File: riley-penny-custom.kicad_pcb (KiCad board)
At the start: 2 copper layers, 110 x 84.3 mm, 4 parts, among them J1 Barrel_Jack_Switch, J2 AudioJack_TRS, J3 AudioJack_TRS

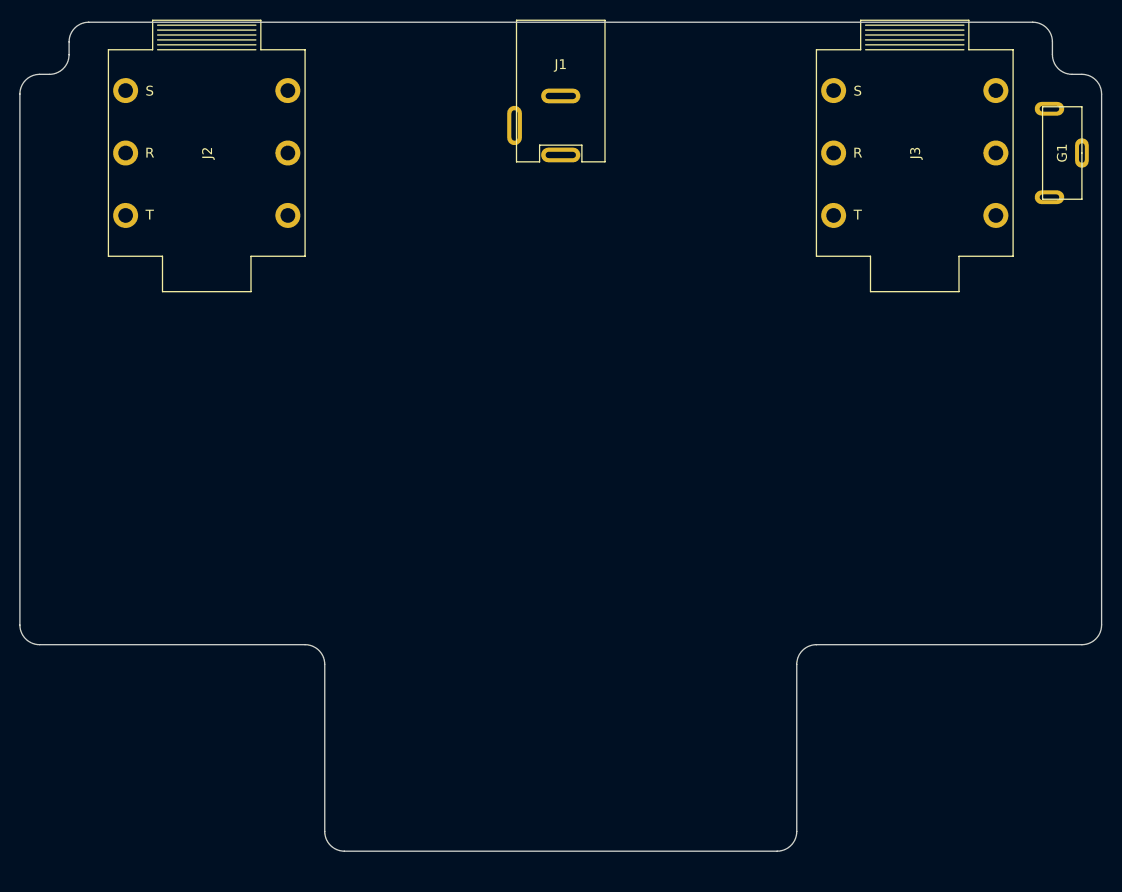
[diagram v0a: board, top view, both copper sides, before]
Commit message: finished schematics, started PCB
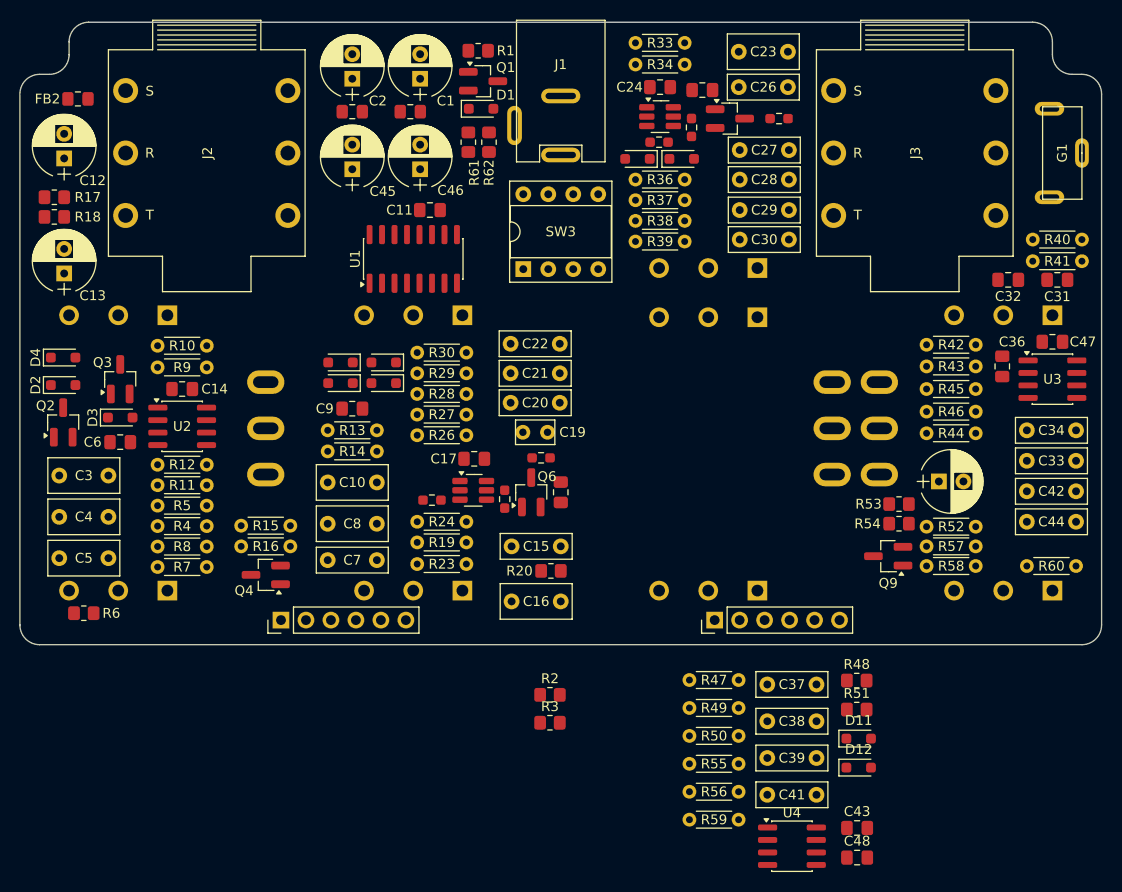
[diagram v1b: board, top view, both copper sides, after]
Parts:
- added C1: 100uF, bca-footprints:CP_Radial_D6.3mm_P2.50mm, F.Cu at (-14.3, -38.8)
- added C10: 0.47uF, bca-footprints:C_Film_L7.2mm_W3.5mm_P5.00mm, F.Cu at (-21.2, 3.50)
- added C11: 1u, Capacitor_SMD:C_0805_2012Metric_Pad1.18x1.45mm_HandSolder, F.Cu at (-13.3, -24.2)
- added C12: 100u, bca-footprints:CP_Radial_D6.3mm_P2.50mm, F.Cu at (-50.5, -30.7)
- added C13: 100u, bca-footprints:CP_Radial_D6.3mm_P2.50mm, F.Cu at (-50.5, -19.0)
- added C14: 100n, Capacitor_SMD:C_0805_2012Metric_Pad1.18x1.45mm_HandSolder, F.Cu at (-38.5, -6.00)
- added C15: 10n, bca-footprints:C_Film_L7.2mm_W2.5mm_P5.00mm, F.Cu at (-2.50, 10.0)
- added C16: 0.15u, bca-footprints:C_Film_L7.2mm_W3.5mm_P5.00mm, F.Cu at (-2.50, 15.6)
- added C17: 47p, Capacitor_SMD:C_0805_2012Metric_Pad1.18x1.45mm_HandSolder, F.Cu at (-8.80, 1.10)
- added C18: 47p, Capacitor_SMD:C_0805_2012Metric_Pad1.18x1.45mm_HandSolder, F.Cu at (0.00, 4.50)
- added C19: 220p, bca-footprints:C_Ceramic_L4.0mm_W2.5mm_P2.50mm, F.Cu at (-2.60, -1.60)
- added C2: 100uF, bca-footprints:CP_Radial_D6.3mm_P2.50mm, F.Cu at (-21.2, -38.8)
- added C20: 0.1u, bca-footprints:C_Film_L7.2mm_W2.5mm_P5.00mm, F.Cu at (-2.60, -4.60)
- added C21: 47n, bca-footprints:C_Film_L7.2mm_W2.5mm_P5.00mm, F.Cu at (-2.60, -7.60)
- added C22: 3.9n, bca-footprints:C_Film_L7.2mm_W2.5mm_P5.00mm, F.Cu at (-2.60, -10.6)
- added C23: 0.47u, bca-footprints:C_Film_L7.2mm_W3.5mm_P5.00mm, F.Cu at (20.6, -40.3)
- added C24: 100p, Capacitor_SMD:C_0805_2012Metric_Pad1.18x1.45mm_HandSolder, F.Cu at (10.1, -36.7)
- added C25: 100p, Capacitor_SMD:C_0805_2012Metric_Pad1.18x1.45mm_HandSolder, F.Cu at (14.4, -36.4)
- added C26: 5.6n, bca-footprints:C_Film_L7.2mm_W2.5mm_P5.00mm, F.Cu at (20.6, -36.7)
- added C27: 5.6n, bca-footprints:C_Film_L7.2mm_W2.5mm_P5.00mm, F.Cu at (20.7, -30.3)
- added C28: 18n, bca-footprints:C_Film_L7.2mm_W2.5mm_P5.00mm, F.Cu at (20.7, -27.3)
- added C29: 68n, bca-footprints:C_Film_L7.2mm_W2.5mm_P5.00mm, F.Cu at (20.7, -24.2)
- added C3: 0.47u, bca-footprints:C_Film_L7.2mm_W3.5mm_P5.00mm, F.Cu at (-48.5, 2.80)
- added C30: 33n, bca-footprints:C_Film_L7.2mm_W2.5mm_P5.00mm, F.Cu at (20.7, -21.2)
- added C31: 22p, Capacitor_SMD:C_0805_2012Metric_Pad1.18x1.45mm_HandSolder, F.Cu at (50.5, -17.1)
- added C32: 10u, Capacitor_SMD:C_0805_2012Metric_Pad1.18x1.45mm_HandSolder, F.Cu at (45.5, -17.1)
- added C33: 8.2n, bca-footprints:C_Film_L7.2mm_W2.5mm_P5.00mm, F.Cu at (49.9, 1.30)
- added C34: 5.6n, bca-footprints:C_Film_L7.2mm_W2.5mm_P5.00mm, F.Cu at (49.9, -1.80)
- added C36: 47p, Capacitor_SMD:C_0805_2012Metric_Pad1.18x1.45mm_HandSolder, F.Cu at (44.9, -8.30)
- added C37: 47n, bca-footprints:C_Film_L7.2mm_W2.5mm_P5.00mm, F.Cu at (23.5, 24.0)
- added C38: 8.2n, bca-footprints:C_Film_L7.2mm_W2.5mm_P5.00mm, F.Cu at (23.5, 27.8)
- added C39: 18n, bca-footprints:C_Film_L7.2mm_W2.5mm_P5.00mm, F.Cu at (23.5, 31.5)
- added C4: 0.22u, bca-footprints:C_Film_L7.2mm_W3.5mm_P5.00mm, F.Cu at (-48.5, 7.00)
- added C40: 100u, bca-footprints:CP_Radial_D6.3mm_P2.50mm, F.Cu at (39.7, 3.40)
- added C41: 3.9n, bca-footprints:C_Film_L7.2mm_W2.5mm_P5.00mm, F.Cu at (23.5, 35.3)
- added C42: 39n, bca-footprints:C_Film_L7.2mm_W2.5mm_P5.00mm, F.Cu at (49.9, 4.40)
- added C43: 10u, Capacitor_SMD:C_0805_2012Metric_Pad1.18x1.45mm_HandSolder, F.Cu at (30.1, 38.6)
- added C44: 5.6n, bca-footprints:C_Film_L7.2mm_W2.5mm_P5.00mm, F.Cu at (49.9, 7.50)
- added C45: 100u, bca-footprints:CP_Radial_D6.3mm_P2.50mm, F.Cu at (-21.2, -29.6)
- added C46: 100u, bca-footprints:CP_Radial_D6.3mm_P2.50mm, F.Cu at (-14.3, -29.6)
- added C47: 100n, Capacitor_SMD:C_0805_2012Metric_Pad1.18x1.45mm_HandSolder, F.Cu at (50.0, -10.8)
- added C48: 100n, Capacitor_SMD:C_0805_2012Metric_Pad1.18x1.45mm_HandSolder, F.Cu at (30.1, 41.6)
- added C5: 0.22u, bca-footprints:C_Film_L7.2mm_W3.5mm_P5.00mm, F.Cu at (-48.5, 11.2)
- added C6: 100p, Capacitor_SMD:C_0805_2012Metric_Pad1.18x1.45mm_HandSolder, F.Cu at (-44.8, -0.60)
- added C7: 3.3nF, bca-footprints:C_Film_L7.2mm_W2.5mm_P5.00mm, F.Cu at (-21.2, 11.4)
- added C8: 0.22uF, bca-footprints:C_Film_L7.2mm_W3.5mm_P5.00mm, F.Cu at (-21.2, 7.70)
- added C9: 470p, Capacitor_SMD:C_0805_2012Metric_Pad1.18x1.45mm_HandSolder, F.Cu at (-21.2, -4.00)
- added D1: 9V1 Zener, Diode_SMD:D_SOD-323_HandSoldering, F.Cu at (-8.10, -34.5)
- added D10: 3v3 Zener, Diode_SMD:D_SOD-323_HandSoldering, F.Cu at (7.80, -29.4)
- added D11: 1N4148, Diode_SMD:D_SOD-323_HandSoldering, F.Cu at (30.3, 29.6)
- added D12: 1N4148, Diode_SMD:D_SOD-323_HandSoldering, F.Cu at (30.3, 32.5)
- added D2: 1N5711, Diode_SMD:D_SOD-323_HandSoldering, F.Cu at (-50.6, -6.40)
- added D3: 1N5711, Diode_SMD:D_SOD-323_HandSoldering, F.Cu at (-44.8, -3.10)
- added D4: 1N5711, Diode_SMD:D_SOD-323_HandSoldering, F.Cu at (-50.6, -9.20)
- added D5: 1N4148, Diode_SMD:D_SOD-323_HandSoldering, F.Cu at (-18.0, -6.60)
- added D6: 1N5711, Diode_SMD:D_SOD-323_HandSoldering, F.Cu at (-22.4, -6.60)
- added D7: 1N4148, Diode_SMD:D_SOD-323_HandSoldering, F.Cu at (-18.0, -8.70)
- added D8: 1N4148, Diode_SMD:D_SOD-323_HandSoldering, F.Cu at (-22.4, -8.70)
- added D9: 3v3 Zener, Diode_SMD:D_SOD-323_HandSoldering, F.Cu at (12.3, -29.4)
- added FB1: FerriteBead_Small, Inductor_SMD:L_0805_2012Metric_Pad1.15x1.40mm_HandSolder, F.Cu at (-15.3, -34.2)
- added FB2: FerriteBead_Small, Inductor_SMD:L_0805_2012Metric_Pad1.15x1.40mm_HandSolder, F.Cu at (-49.1, -35.5)
- added FB3: FerriteBead_Small, Inductor_SMD:L_0805_2012Metric_Pad1.15x1.40mm_HandSolder, F.Cu at (-21.2, -34.2)
- added J4: Conn_01x06, bca-footprints:Pin_Header_Straight_1x06_Pitch2.54mm, F.Cu at (-22.1, 17.5)
- added J5: Conn_01x06, bca-footprints:Pin_Header_Straight_1x06_Pitch2.54mm, F.Cu at (22.0, 17.5)
- added Q1: Q_PMOS_GSD, Package_TO_SOT_SMD:SOT-23_Handsoldering, F.Cu at (-7.90, -37.3)
- added Q2: 2N7002, Package_TO_SOT_SMD:SOT-23_Handsoldering, F.Cu at (-50.6, -2.60)
- added Q3: 2N7002, Package_TO_SOT_SMD:SOT-23_Handsoldering, F.Cu at (-44.8, -7.00)
- added Q4: 2N7002, Package_TO_SOT_SMD:SOT-23_Handsoldering, F.Cu at (-30.0, 12.9)
- added Q5: LS844, Package_TO_SOT_SMD:SOT-23-6_Handsoldering, F.Cu at (-8.90, 4.30)
- added Q6: BC858C, Package_TO_SOT_SMD:SOT-23_Handsoldering, F.Cu at (-3.00, 4.50)
- added Q7: LS844, Package_TO_SOT_SMD:SOT-23-6_Handsoldering, F.Cu at (10.1, -33.7)
- added Q8: BC858C, Package_TO_SOT_SMD:SOT-23_Handsoldering, F.Cu at (17.2, -33.5)
- added Q9: BC848C, Package_TO_SOT_SMD:SOT-23_Handsoldering, F.Cu at (33.3, 11.0)
- added R1: 10k, Resistor_SMD:R_0805_2012Metric_Pad1.20x1.40mm_HandSolder, F.Cu at (-8.40, -40.4)
- added R10: 10k, bca-footprints:R_L3.6mm_D1.6mm_P5.00mm_Horizontal, F.Cu at (-38.5, -10.4)
- added R11: 10k, bca-footprints:R_L3.6mm_D1.6mm_P5.00mm_Horizontal, F.Cu at (-38.5, 3.78)
- added R12: 18k, bca-footprints:R_L3.6mm_D1.6mm_P5.00mm_Horizontal, F.Cu at (-38.5, 1.70)
- added R13: 10k, bca-footprints:R_L3.6mm_D1.6mm_P5.00mm_Horizontal, F.Cu at (-21.2, -1.80)
- added R14: 1k, bca-footprints:R_L3.6mm_D1.6mm_P5.00mm_Horizontal, F.Cu at (-21.2, 0.34)
- added R15: 100k, bca-footprints:R_L3.6mm_D1.6mm_P5.00mm_Horizontal, F.Cu at (-30.0, 7.90)
- added R16: 100k, bca-footprints:R_L3.6mm_D1.6mm_P5.00mm_Horizontal, F.Cu at (-30.0, 10.0)
- added R17: 10k, Resistor_SMD:R_0805_2012Metric_Pad1.20x1.40mm_HandSolder, F.Cu at (-51.5, -25.5)
- added R18: 10k, Resistor_SMD:R_0805_2012Metric_Pad1.20x1.40mm_HandSolder, F.Cu at (-51.5, -23.5)
- added R19: 10k, bca-footprints:R_L3.6mm_D1.6mm_P5.00mm_Horizontal, F.Cu at (-12.1, 9.60)
- added R2: 22k, Resistor_SMD:R_0805_2012Metric_Pad1.20x1.40mm_HandSolder, F.Cu at (-1.10, 25.1)
- added R20: 1M, Resistor_SMD:R_0805_2012Metric_Pad1.20x1.40mm_HandSolder, F.Cu at (-1.00, 12.5)
- added R21: 2.2k, Resistor_SMD:R_0603_1608Metric_Pad0.98x0.95mm_HandSolder, F.Cu at (-5.70, 5.20)
- added R22: 4.7k, Resistor_SMD:R_0603_1608Metric_Pad0.98x0.95mm_HandSolder, F.Cu at (-13.1, 5.30)
- added R23: 1.5k, bca-footprints:R_L3.6mm_D1.6mm_P5.00mm_Horizontal, F.Cu at (-12.1, 11.8)
- added R24: 15k, bca-footprints:R_L3.6mm_D1.6mm_P5.00mm_Horizontal, F.Cu at (-12.1, 7.50)
- added R25: 2.2k, Resistor_SMD:R_0603_1608Metric_Pad0.98x0.95mm_HandSolder, F.Cu at (-2.00, 1.00)
- added R26: 56k, bca-footprints:R_L3.6mm_D1.6mm_P5.00mm_Horizontal, F.Cu at (-12.1, -1.30)
- added R27: 330k, bca-footprints:R_L3.6mm_D1.6mm_P5.00mm_Horizontal, F.Cu at (-12.1, -3.40)
- added R28: 1M, bca-footprints:R_L3.6mm_D1.6mm_P5.00mm_Horizontal, F.Cu at (-12.1, -5.50)
- added R29: 15k, bca-footprints:R_L3.6mm_D1.6mm_P5.00mm_Horizontal, F.Cu at (-12.1, -7.60)
- added R3: 22k, Resistor_SMD:R_0805_2012Metric_Pad1.20x1.40mm_HandSolder, F.Cu at (-1.10, 27.9)
- added R30: 470k, bca-footprints:R_L3.6mm_D1.6mm_P5.00mm_Horizontal, F.Cu at (-12.1, -9.70)
- added R31: 2.2k, Resistor_SMD:R_0603_1608Metric_Pad0.98x0.95mm_HandSolder, F.Cu at (13.3, -32.6)
- added R32: 4.7k, Resistor_SMD:R_0603_1608Metric_Pad0.98x0.95mm_HandSolder, F.Cu at (10.0, -31.1)
- added R33: 3.9k, bca-footprints:R_L3.6mm_D1.6mm_P5.00mm_Horizontal, F.Cu at (10.1, -41.2)
- added R34: 33k, bca-footprints:R_L3.6mm_D1.6mm_P5.00mm_Horizontal, F.Cu at (10.1, -39.0)
- added R35: 2.2k, Resistor_SMD:R_0603_1608Metric_Pad0.98x0.95mm_HandSolder, F.Cu at (22.2, -33.5)
- added R36: 1k, bca-footprints:R_L3.6mm_D1.6mm_P5.00mm_Horizontal, F.Cu at (10.1, -27.3)
- added R37: 6.8k, bca-footprints:R_L3.6mm_D1.6mm_P5.00mm_Horizontal, F.Cu at (10.1, -25.2)
- added R38: 5.6k, bca-footprints:R_L3.6mm_D1.6mm_P5.00mm_Horizontal, F.Cu at (10.1, -23.1)
- added R39: 3.9k, bca-footprints:R_L3.6mm_D1.6mm_P5.00mm_Horizontal, F.Cu at (10.1, -21.0)
- added R4: 2.2M, bca-footprints:R_L3.6mm_D1.6mm_P5.00mm_Horizontal, F.Cu at (-38.5, 7.94)
- added R40: 470k, bca-footprints:R_L3.6mm_D1.6mm_P5.00mm_Horizontal, F.Cu at (50.5, -21.2)
- added R41: 180k, bca-footprints:R_L3.6mm_D1.6mm_P5.00mm_Horizontal, F.Cu at (50.5, -19.0)
- added R42: 10k, bca-footprints:R_L3.6mm_D1.6mm_P5.00mm_Horizontal, F.Cu at (39.7, -10.5)
- added R43: 22k, bca-footprints:R_L3.6mm_D1.6mm_P5.00mm_Horizontal, F.Cu at (39.7, -8.30)
- added R44: 15k, bca-footprints:R_L3.6mm_D1.6mm_P5.00mm_Horizontal, F.Cu at (39.7, -1.50)
- added R45: 10k, bca-footprints:R_L3.6mm_D1.6mm_P5.00mm_Horizontal, F.Cu at (39.7, -6.00)
- added R46: 22k, bca-footprints:R_L3.6mm_D1.6mm_P5.00mm_Horizontal, F.Cu at (39.7, -3.70)
- added R47: 1.5k, bca-footprints:R_L3.6mm_D1.6mm_P5.00mm_Horizontal, F.Cu at (15.6, 23.6)
- added R48: 1M, Resistor_SMD:R_0805_2012Metric_Pad1.20x1.40mm_HandSolder, F.Cu at (30.1, 23.6)
- added R49: 470k, bca-footprints:R_L3.6mm_D1.6mm_P5.00mm_Horizontal, F.Cu at (15.6, 26.4)
- added R5: 470k, bca-footprints:R_L3.6mm_D1.6mm_P5.00mm_Horizontal, F.Cu at (-38.5, 5.86)
- added R50: 1k, bca-footprints:R_L3.6mm_D1.6mm_P5.00mm_Horizontal, F.Cu at (15.6, 29.3)
- added R51: 1M, Resistor_SMD:R_0805_2012Metric_Pad1.20x1.40mm_HandSolder, F.Cu at (30.1, 26.6)
- added R52: 22k, bca-footprints:R_L3.6mm_D1.6mm_P5.00mm_Horizontal, F.Cu at (39.7, 8.00)
- added R53: 1M, Resistor_SMD:R_0805_2012Metric_Pad1.20x1.40mm_HandSolder, F.Cu at (34.4, 5.70)
- added R54: 1M, Resistor_SMD:R_0805_2012Metric_Pad1.20x1.40mm_HandSolder, F.Cu at (34.4, 7.70)
- added R55: 6.8k, bca-footprints:R_L3.6mm_D1.6mm_P5.00mm_Horizontal, F.Cu at (15.6, 32.1)
- added R56: 100k, bca-footprints:R_L3.6mm_D1.6mm_P5.00mm_Horizontal, F.Cu at (15.6, 35.0)
- added R57: 470k, bca-footprints:R_L3.6mm_D1.6mm_P5.00mm_Horizontal, F.Cu at (39.7, 10.0)
- added R58: 1k, bca-footprints:R_L3.6mm_D1.6mm_P5.00mm_Horizontal, F.Cu at (39.7, 12.0)
- added R59: 10k, bca-footprints:R_L3.6mm_D1.6mm_P5.00mm_Horizontal, F.Cu at (15.6, 37.8)
- added R6: 10M, Resistor_SMD:R_0805_2012Metric_Pad1.20x1.40mm_HandSolder, F.Cu at (-48.5, 16.8)
- added R60: 10k, bca-footprints:R_L3.6mm_D1.6mm_P5.00mm_Horizontal, F.Cu at (49.9, 12.0)
- added R61: 10k, Resistor_SMD:R_0805_2012Metric_Pad1.20x1.40mm_HandSolder, F.Cu at (-9.40, -31.1)
- added R62: 10k, Resistor_SMD:R_0805_2012Metric_Pad1.20x1.40mm_HandSolder, F.Cu at (-7.30, -31.1)
- added R7: 10k, bca-footprints:R_L3.6mm_D1.6mm_P5.00mm_Horizontal, F.Cu at (-38.5, 12.1)
- added R8: 1k, bca-footprints:R_L3.6mm_D1.6mm_P5.00mm_Horizontal, F.Cu at (-38.5, 10.0)
- added R9: 680k, bca-footprints:R_L3.6mm_D1.6mm_P5.00mm_Horizontal, F.Cu at (-38.5, -8.20)
- added RV1: 10kC, bca-footprints:R_POT, F.Cu at (-45.0, -2.00)
- added RV2: 1MA, bca-footprints:R_POT, F.Cu at (-45.0, -30.0)
- added RV3: 50kB, bca-footprints:R_POT, F.Cu at (-15.0, -2.00)
- added RV4: 100kA, bca-footprints:R_POT, F.Cu at (-15.0, -30.0)
- added RV5: 250kA, bca-footprints:R_POT_DUAL, F.Cu at (15.0, -30.0)
- added RV6: 100kA, bca-footprints:R_POT, F.Cu at (45.0, -30.0)
- added RV7: 100k-CD, bca-footprints:R_POT, F.Cu at (15.0, -2.00)
- added RV8: 100k-CD, bca-footprints:R_POT, F.Cu at (45.0, -2.00)
- added SW1: SW_SPDT, bca-footprints:SW_Toggle_SPDT_SolderLug, B.Cu at (-30.0, -2.00)
- added SW2: SW_DPDT_x2, bca-footprints:SW_Toggle_DPDT_SolderLug, B.Cu at (30.0, -2.00)
- added SW3: SW_DIP_SPDT_2pos, bca-footprints:DIP-8_W7.62mm_Socket, F.Cu at (0.00, -22.0)
- added U1: DG412xY, Package_SO:SOIC-16_3.9x9.9mm_P1.27mm, F.Cu at (-15.0, -19.2)
- added U2: OPA2134, Package_SO:SOIC-8_3.9x4.9mm_P1.27mm, F.Cu at (-38.5, -2.20)
- added U3: TLV9352, Package_SO:SOIC-8_3.9x4.9mm_P1.27mm, F.Cu at (50.0, -7.00)
- added U4: TLV9352, Package_SO:SOIC-8_3.9x4.9mm_P1.27mm, F.Cu at (23.5, 40.5)
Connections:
- J1 pad 1: Net-(J1-Pad1) -> Earth
- J1 pad 3: Net-(J1-Pad3) -> unconnected-(J1-Pad3)
- J2 pad 2: Net-(J1-Pad1) -> Earth
- J2 pad 5: Net-(J2-Pad5) -> Earth
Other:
- board size 110 x 84.3 mm -> 110 x 63.3 mm

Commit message: initial layout
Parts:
- removed C46: 100u, bca-footprints:CP_Radial_D6.3mm_P2.50mm
- removed C47, C48: 100n, Capacitor_SMD:C_0805_2012Metric_Pad1.18x1.45mm_HandSolder
- removed R62: 10k, Resistor_SMD:R_0805_2012Metric_Pad1.20x1.40mm_HandSolder
- added C35: 47p, Capacitor_SMD:C_0603_1608Metric_Pad1.08x0.95mm_HandSolder, F.Cu at (48.7, -1.20)
- C14, C17, C18, C24, C25, C31, C6, C9: footprint Capacitor_SMD:C_0805_2012Metric_Pad1.18x1.45mm_HandSolder -> Capacitor_SMD:C_0603_1608Metric_Pad1.08x0.95mm_HandSolder
- C23: value 0.47u -> 1u
- C33: value 8.2n -> 5.6n
- C34: value 5.6n -> 8.2n
- C36: value 47p -> 8.2n; footprint Capacitor_SMD:C_0805_2012Metric_Pad1.18x1.45mm_HandSolder -> bca-footprints:C_Film_L7.2mm_W2.5mm_P5.00mm
- C37: value 47n -> 18n
- C38: value 8.2n -> 39n
- C39: value 18n -> 3.9n
- C40: value 100u -> 5.6n; footprint bca-footprints:CP_Radial_D6.3mm_P2.50mm -> bca-footprints:C_Film_L7.2mm_W2.5mm_P5.00mm
- C41: value 3.9n -> 10u; footprint bca-footprints:C_Film_L7.2mm_W2.5mm_P5.00mm -> Capacitor_SMD:C_0805_2012Metric_Pad1.18x1.45mm_HandSolder
- C42: value 39n -> 100u; footprint bca-footprints:C_Film_L7.2mm_W2.5mm_P5.00mm -> bca-footprints:CP_Radial_D6.3mm_P2.50mm
- C43: value 10u -> 100u; footprint Capacitor_SMD:C_0805_2012Metric_Pad1.18x1.45mm_HandSolder -> bca-footprints:CP_Radial_D6.3mm_P2.50mm
- C44: value 5.6n -> 100n; footprint bca-footprints:C_Film_L7.2mm_W2.5mm_P5.00mm -> Capacitor_SMD:C_0603_1608Metric_Pad1.08x0.95mm_HandSolder
- C45: value 100u -> 100n; footprint bca-footprints:CP_Radial_D6.3mm_P2.50mm -> Capacitor_SMD:C_0603_1608Metric_Pad1.08x0.95mm_HandSolder
- D10: value 3v3 Zener -> 4v7 Zener
- R48: value 1M -> 470k; footprint Resistor_SMD:R_0805_2012Metric_Pad1.20x1.40mm_HandSolder -> bca-footprints:R_L3.6mm_D1.6mm_P5.00mm_Horizontal
- R49: value 470k -> 1M; footprint bca-footprints:R_L3.6mm_D1.6mm_P5.00mm_Horizontal -> Resistor_SMD:R_0805_2012Metric_Pad1.20x1.40mm_HandSolder
- R52: value 22k -> 33k; footprint bca-footprints:R_L3.6mm_D1.6mm_P5.00mm_Horizontal -> Resistor_SMD:R_0805_2012Metric_Pad1.20x1.40mm_HandSolder
- R54: value 1M -> 6.8k; footprint Resistor_SMD:R_0805_2012Metric_Pad1.20x1.40mm_HandSolder -> bca-footprints:R_L3.6mm_D1.6mm_P5.00mm_Horizontal
- R55: value 6.8k -> 470k
- R56: value 100k -> 1k
- R57: value 470k -> 100k
- R58: value 1k -> 10k
- R60: footprint bca-footprints:R_L3.6mm_D1.6mm_P5.00mm_Horizontal -> Resistor_SMD:R_0805_2012Metric_Pad1.20x1.40mm_HandSolder
- moved C43 81.4 mm to (-14.3, -29.5), turned to 90 degrees
- moved C42 78.7 mm to (-21.2, -29.4), turned to 90 degrees
- moved R60 73.3 mm to (-9.40, -31.1), turned to 90 degrees
- moved R3 50.8 mm to (-7.30, -22.5), turned to 90 degrees
- moved R2 48.3 mm to (-9.40, -22.5), turned to 90 degrees
- moved U4 46.7 mm to (20.0, -6.10), turned to 90 degrees
- moved C45 43.5 mm to (16.4, -7.70), turned to -90 degrees
- moved R50 42.1 mm to (40.8, -4.40), turned to 180 degrees
- moved R49 41.6 mm to (33.8, -11.0), turned to 90 degrees
- moved R56 38.5 mm to (10.1, -3.20)
- moved C37 38.4 mm to (40.8, -10.2)
- moved R51 37.6 mm to (31.3, -11.0), turned to -90 degrees
- moved R47 36.0 mm to (40.8, -2.17), turned to 180 degrees
- moved C41 35.4 mm to (17.6, 0.40), turned to -90 degrees
- moved R58 34.3 mm to (10.1, -5.40), turned to 180 degrees
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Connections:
- C33 pad 1: Net-(C33-Pad1) -> Net-(U3A--)
- C34 pad 1: Net-(U3A--) -> Net-(C34-Pad1)
- C36 pad 1: Net-(U3A--) -> Net-(U4B-+)
- C37 pad 2: Net-(C37-Pad2) -> Net-(SW2A-C)
- C38 pad 1: Net-(U4B-+) -> Net-(SW2B-A)
- C39 pad 1: Net-(C38-Pad2) -> Net-(D11-K)
- C39 pad 2: Net-(SW2A-C) -> Net-(C39-Pad2)
- C40 pad 1: Net-(SW2B-C) -> Net-(C38-Pad2)
- C40 pad 2: Net-(C40-Pad2) -> Net-(Q9-B)
- C41 pad 1: Net-(D11-K) -> Net-(C39-Pad2)
- C42 pad 1: Net-(SW2B-A) -> /blues-driver/9V
- C42 pad 2: Net-(C42-Pad2) -> Earth
- C43 pad 1: Net-(C41-Pad2) -> /blues-driver/4.5V
- C43 pad 2: Net-(C43-Pad2) -> Earth
- C44 pad 1: Net-(C42-Pad2) -> /blues-driver/9V
- C44 pad 2: Net-(Q9-B) -> Earth
- R43 pad 2: Net-(C33-Pad2) -> Net-(C34-Pad2)
- R45 pad 2: Net-(C36-Pad2) -> Net-(C35-Pad2)
- R46 pad 1: Net-(C33-Pad1) -> Net-(C34-Pad1)
- R46 pad 2: Net-(C36-Pad2) -> Net-(C35-Pad2)
- R47 pad 1: Net-(C37-Pad2) -> Net-(C35-Pad2)
- R48 pad 1: Net-(U4B-+) -> /blues-driver/4.5V
- R48 pad 2: /blues-driver/4.5V -> Net-(D11-A)
- R49 pad 1: /blues-driver/4.5V -> Net-(U4B-+)
- R49 pad 2: Net-(D11-A) -> /blues-driver/4.5V
- R50 pad 1: Net-(C38-Pad2) -> Net-(C36-Pad2)
- R52 pad 1: Earth -> /blues-driver/4.5V
- R52 pad 2: Net-(C40-Pad2) -> Net-(SW2A-A)
- R53 pad 2: Net-(SW2B-C) -> Net-(SW2B-A)
- R54 pad 1: /blues-driver/4.5V -> Net-(D11-K)
- R54 pad 2: Net-(SW2B-A) -> Net-(C39-Pad2)
- R55 pad 1: Net-(D11-K) -> Net-(Q9-B)
- R55 pad 2: Net-(C41-Pad2) -> /blues-driver/4.5V
- R56 pad 1: Earth -> Net-(Q9-E)
- R56 pad 2: Net-(C43-Pad2) -> Net-(C38-Pad2)
- R57 pad 1: Net-(Q9-B) -> Earth
- R57 pad 2: /blues-driver/4.5V -> Net-(C41-Pad2)
- R58 pad 1: Net-(Q9-E) -> Earth
- R58 pad 2: Net-(C42-Pad2) -> Net-(Q9-E)
- R59 pad 1: Net-(C43-Pad2) -> Net-(C41-Pad2)
- R60 pad 1: Earth -> /blues-driver/4.5V
- R60 pad 2: Net-(Q9-E) -> /blues-driver/9V
- R61 pad 1: /blues-driver/4.5V -> Earth
- R61 pad 2: /blues-driver/9V -> /blues-driver/4.5V
- RV7 pad 2: Net-(C34-Pad2) -> Net-(C33-Pad2)
- RV8 pad 1: Net-(C33-Pad1) -> Net-(C34-Pad1)
- RV8 pad 3: Net-(C33-Pad2) -> Net-(C34-Pad2)
- SW2 pad 1: unconnected-(SW2A-A-Pad1) -> Net-(SW2A-A)
- SW2 pad 6: Net-(SW2B-C) -> unconnected-(SW2B-C-Pad6)
- U3 pad 1: Net-(C36-Pad2) -> Net-(C35-Pad2)
- U4 pad 1: Net-(C41-Pad2) -> Net-(C39-Pad2)
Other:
- outline, holes or cut-outs redrawn

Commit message: first draft PCB
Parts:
- C15: value 10n -> 18n
- C31: value 22p -> 47p
- C32, C41: footprint Capacitor_SMD:C_0805_2012Metric_Pad1.18x1.45mm_HandSolder -> Capacitor_SMD:C_1206_3216Metric_Pad1.33x1.80mm_HandSolder
- C33: value 5.6n -> 3.9n
- C34: value 8.2n -> 15n
- C37: value 18n -> 15n
- C38: value 39n -> 33n
- D10: value 4v7 Zener -> 4v7 Z; footprint Diode_SMD:D_SOD-323_HandSoldering -> bca-footprints:Diode_Zener_DO-35_P5.00mm
- D11, D12, D2, D3, D4, D5, D6, D7, D8: footprint Diode_SMD:D_SOD-323_HandSoldering -> bca-footprints:Diode_DO-35_P5.00mm
- D9: value 3v3 Zener -> 3v3 Z; footprint Diode_SMD:D_SOD-323_HandSoldering -> bca-footprints:Diode_Zener_DO-35_P5.00mm
- R33: value 3.9k -> 2.2k
- R34: value 33k -> 22k
- R42, R45: value 10k -> 15k
- R44: value 15k -> 10k
- R47: value 1.5k -> 6.8k
- R53: value 1M -> 56k; footprint Resistor_SMD:R_0805_2012Metric_Pad1.20x1.40mm_HandSolder -> bca-footprints:R_L3.6mm_D1.6mm_P5.00mm_Horizontal
- R56: value 1k -> 1.5k
- moved D9 22.1 mm to (10.0, -7.40), turned to 180 degrees
- moved D10 19.4 mm to (10.0, -10.1)
- moved R52 18.4 mm to (27.6, -11.0), turned to -90 degrees
- moved R53 14.5 mm to (19.9, 10.9), turned to 0 degrees
- moved R13 13.2 mm to (-30.0, -12.8), turned to 180 degrees
- moved R14 13.2 mm to (-30.0, -10.6)
- moved C9 13.2 mm to (-30.0, -14.7), turned to 180 degrees
- moved R20 9.14 mm to (0.00, 16.7), turned to 0 degrees
- moved D6 8.65 mm to (-16.5, -6.05), turned to 180 degrees
- moved D5 6.82 mm to (-16.5, -8.50), turned to 180 degrees
- moved C38 6.00 mm to (10.0, 10.9)
- moved C40 5.90 mm to (10.0, 7.50)
- moved Q3 5.66 mm to (-45.6, -1.40), turned to 0 degrees
- moved R55 5.63 mm to (10.0, 4.53)
- moved R56 5.21 mm to (10.0, 2.01)
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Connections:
- C22 pad 2: Net-(Q7B-G1) -> Net-(Q7A-G1)
- C25 pad 1: Net-(Q7B-D2) -> Net-(Q7A-D1)
- C37 pad 2: Net-(SW2A-C) -> Net-(SW2B-C)
- C38 pad 1: Net-(SW2B-A) -> Net-(SW2A-A)
- Q7 pad 1: Net-(D9-A) -> Net-(Q7A-G1)
- Q7 pad 2: /blues-driver/9V -> Net-(Q7A-D1)
- Q7 pad 4: Net-(Q7B-G1) -> Net-(D9-A)
- Q7 pad 5: Net-(Q7B-D2) -> /blues-driver/9V
- Q8 pad 1: Net-(Q7B-D2) -> Net-(Q7A-D1)
- R30 pad 2: Net-(Q7B-G1) -> Net-(Q7A-G1)
- R31 pad 1: Net-(Q7B-D2) -> Net-(Q7A-D1)
- R51 pad 2: Net-(SW2A-C) -> Net-(SW2B-C)
- R52 pad 2: Net-(SW2A-A) -> Net-(SW2A-C)
- R53 pad 2: Net-(SW2B-A) -> Net-(SW2A-A)
- SW2 pad 2: Net-(D11-A) -> Net-(D11-K)
- SW2 pad 4: Net-(SW2B-A) -> unconnected-(SW2B-A-Pad4)
- SW2 pad 5: Net-(D11-K) -> Net-(D11-A)
- SW2 pad 6: unconnected-(SW2B-C-Pad6) -> Net-(SW2B-C)
- U1 pad 1: /Zendrive/Q1D -> /Zendrive/Q1G
- U1 pad 10: Net-(D2-A) -> Net-(C4-Pad1)
- U1 pad 11: Net-(D4-A) -> Earth
- U1 pad 14: (no net) -> Net-(D4-A)
- U1 pad 15: (no net) -> Net-(D2-A)
- U1 pad 16: (no net) -> /Zendrive/Q1D
- U1 pad 2: Net-(C4-Pad1) -> Net-(R9-Pad2)
- U1 pad 3: Earth -> Net-(D4-A)
- U1 pad 6: Net-(R9-Pad2) -> (no net)
- U1 pad 7: Net-(D4-A) -> (no net)
- U1 pad 8: /Zendrive/Q1G -> (no net)
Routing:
- net /blues-driver/4.5V: track 0.00 -> 207.1 mm, vias 0 -> 6
- net /blues-driver/9V: track 0.00 -> 202.2 mm, vias 0 -> 9
- net /Zendrive/9V: track 0.00 -> 98.6 mm, vias 0 -> 2
- net Net-(C4-Pad1): track 0.00 -> 87.6 mm
- net /V+1: track 0.00 -> 86.8 mm, vias 0 -> 1
- net /output_jack: track 0.00 -> 82.7 mm
- net /blues-driver/sw_8: track 0.00 -> 77.4 mm, vias 0 -> 1
- net /Zendrive/4.5V: track 0.00 -> 75.8 mm
- net +9V: track 0.00 -> 72.5 mm
- net /input_jack: track 0.00 -> 71.2 mm
- net Net-(D4-A): track 0.00 -> 67.8 mm, vias 0 -> 1
- net Net-(D3-A): track 0.00 -> 64.2 mm
- net /zendrive_return: track 0.00 -> 61.3 mm
- net Net-(D9-A): track 0.00 -> 61.0 mm, vias 0 -> 3
- net /V+0: track 0.00 -> 51.7 mm, vias 0 -> 1
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- added copper zone on In1.Cu, net Earth
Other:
- copper layers 2 -> 4

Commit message: generated production files
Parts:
- C11, C23: value 1u -> 1uF
- C12, C13, C42, C43: value 100u -> 100uF
- C14, C44, C45: value 100n -> 100nF
- C15, C28: value 18n -> 18nF
- C16: value 0.15u -> 0.15uF
- C17, C18, C31, C35: value 47p -> 47pF
- C19: value 220p -> 220pF
- C20: value 0.1u -> 0.1uF
- C21: value 47n -> 47nF
- C22, C33, C39: value 3.9n -> 3.9nF
- C24, C25, C6: value 100p -> 100pF
- C26, C27, C40: value 5.6n -> 5.6nF
- C29: value 68n -> 68nF
- C3: value 0.47u -> 0.47uF
- C30, C38: value 33n -> 33nF
- C32, C41: value 10u -> 10uF; footprint Capacitor_SMD:C_1206_3216Metric_Pad1.33x1.80mm_HandSolder -> bca-footprints:CP_Radial_D4.0mm_P1.50mm
- C34, C37: value 15n -> 15nF
- C36: value 8.2n -> 8.2nF
- C4, C5: value 0.22u -> 0.22uF
- C9: value 470p -> 470pF
- D10: value 4v7 Z -> 4v7 Zener
- D9: value 3v3 Z -> 3v3 Zener
- Q6, Q8: value BC858C -> BC857C
- Q9: value BC848C -> BC847C
- moved C32 27.6 mm to (33.3, 7.80), turned to -90 degrees
- moved C41 7.75 mm to (26.7, 7.78), turned to -90 degrees
- moved C35 0.80 mm to (48.7, -0.40)
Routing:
- net Net-(C31-Pad2): track 14.7 -> 42.5 mm
- net /blues-driver/vol_out: track 45.0 -> 22.5 mm, vias 0 -> 1
- net Net-(R42-Pad2): track 44.1 -> 52.6 mm
- net Net-(C39-Pad2): track 35.4 -> 41.2 mm
- net Net-(C35-Pad2): track 25.1 -> 27.7 mm
- net Net-(R44-Pad1): track 17.2 -> 19.4 mm
- net Net-(C34-Pad1): track 15.0 -> 17.0 mm
- net Net-(SW2A-A): track 24.0 -> 25.6 mm
- net Net-(C41-Pad2): track 9.46 -> 11.0 mm
- net Net-(D11-K): vias 0 -> 1
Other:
- board text added: "BCA Custom Dual v1.0.0; Mar 2026"
- board text added: "Designed in St. John's, NL"
- board text added: "^fat"
- board text added: "smooth^"

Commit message: re-generated gerbers, finalized BOM
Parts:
- moved FB2 2.81 mm to (-51.9, -35.3)
- moved R41 2.64 mm to (52.6, -20.6), turned to 90 degrees
- moved J2 2.00 mm to (-38.0, -30.0)
- moved J3 2.00 mm to (38.0, -30.0)
- moved C12 1.00 mm to (-51.5, -30.7)
- moved C13 1.00 mm to (-51.5, -19.0)
- moved C31 0.80 mm to (50.5, -16.3)
- moved R40 0.67 mm to (50.2, -20.6), turned to -90 degrees
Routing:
- net Net-(C31-Pad2): track 42.5 -> 50.3 mm
- net /Zendrive/9V: track 98.6 -> 94.5 mm
- net Net-(R40-Pad1): track 10.1 -> 13.1 mm
- net /input_jack: track 71.2 -> 69.2 mm
- net Net-(U3B--): track 14.4 -> 12.8 mm
- net +9V: track 72.5 -> 73.9 mm
- net /output_jack: track 82.7 -> 81.8 mm
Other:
- board text added: "FAT"
- board text added: "SMOOTH"
- board text removed: "^fat"
- board text removed: "smooth^"
